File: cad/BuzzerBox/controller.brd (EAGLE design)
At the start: 100 x 100 mm, 132 parts, among them J2 RASPBERRYPI-40-PIN-GPIO_PTH_N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, Q1 BSS138, Q2 BSS138, Q3 BSS138, T1 BC849, T10 BC849, T2 BC849, T3 BC849, T4 BC849, T5 BC849, T6 BC849, T7 BC849, T8 BC849, T9 BC849, U1 ATMEGA328P-AU, Y1 16MHz

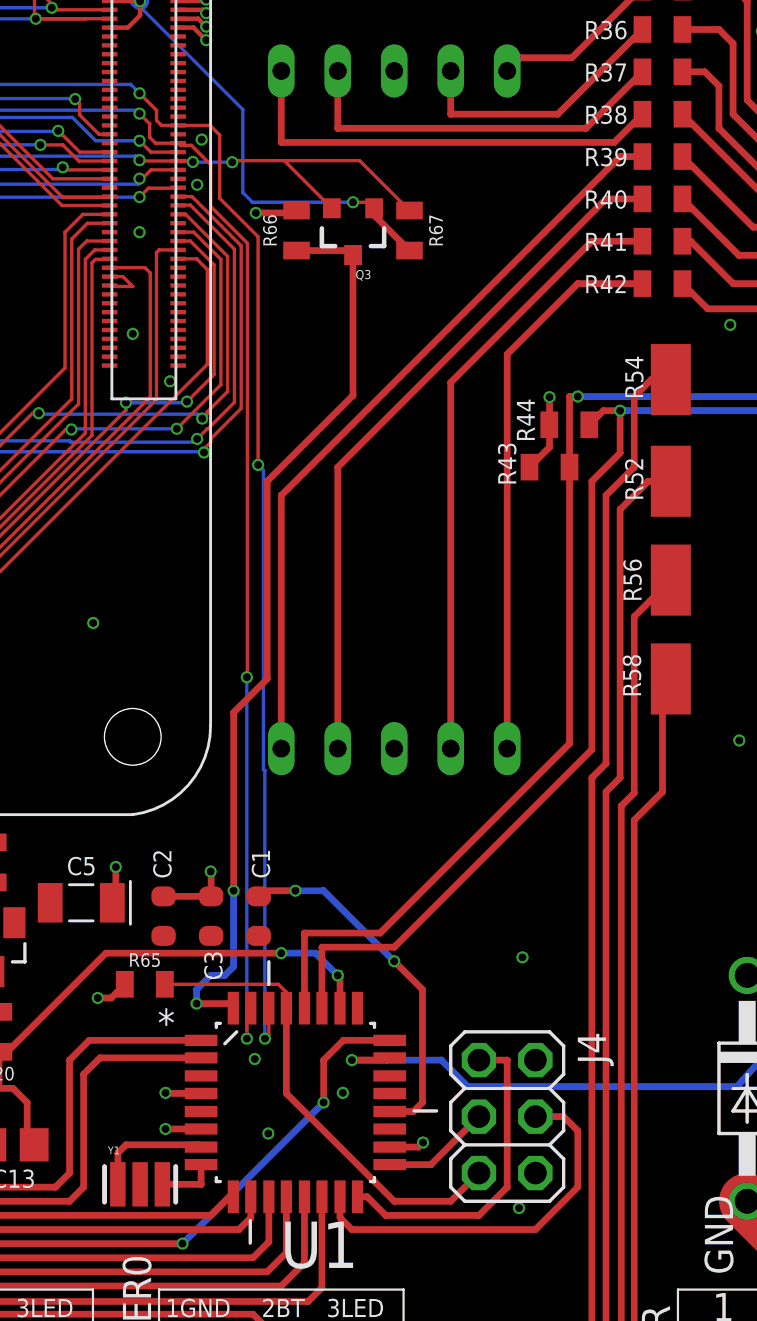
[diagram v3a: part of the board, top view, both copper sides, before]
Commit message: Add level shifter for TX/RX
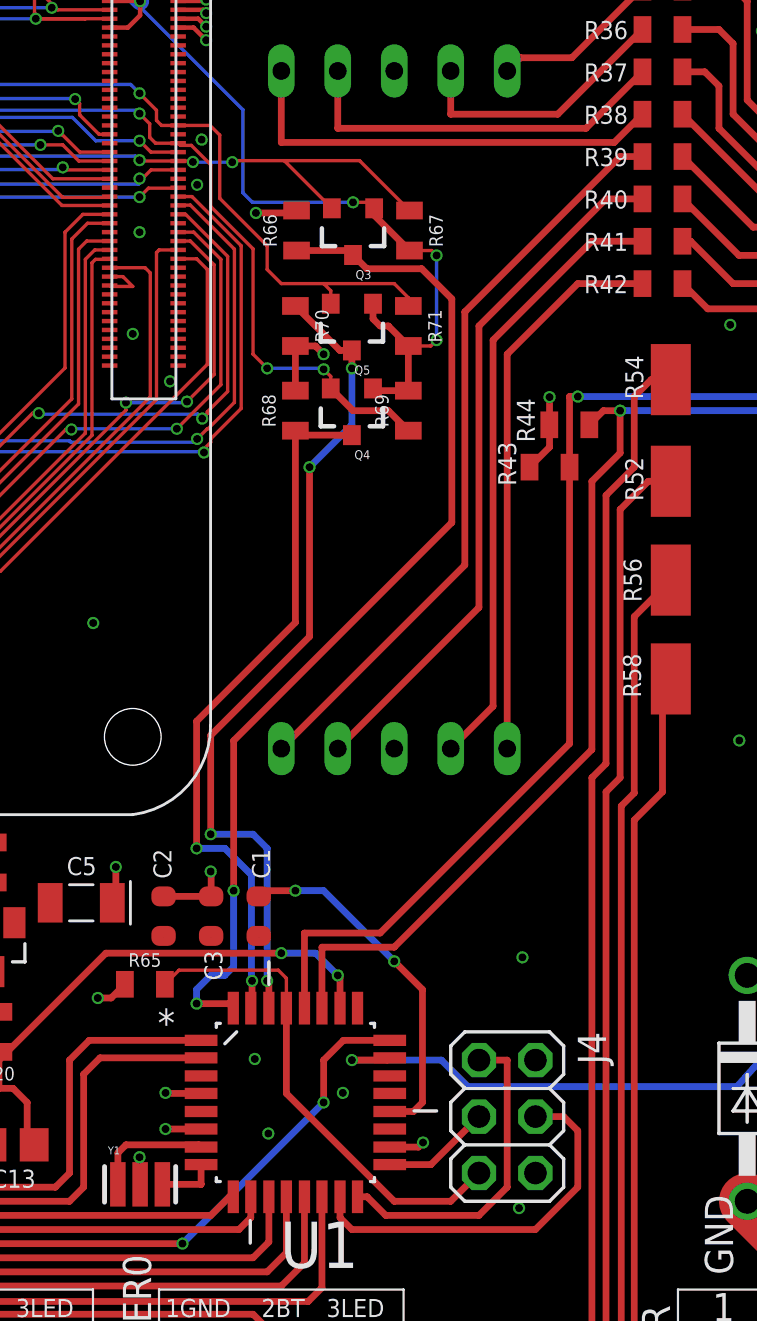
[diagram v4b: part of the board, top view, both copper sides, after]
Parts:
- added Q4, Q5: BSS138, SparkFun:SOT23-3
- added R68, R69, R70, R71: 10K, SparkFun-Resistors:0805
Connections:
- new net RX: Q5.3, R70.1, U1.30
- new net TX: Q4.3, R68.1, U1.31
- net +3V3: now also Q4.1, Q5.1, R69.2, R71.2
- net +5V: now also R68.2, R70.2
- net RXD: now also J2.10, Q4.2, R69.1, RPI-CM4.51; no longer J2.8, RPI-CM4.55, U1.30
- net TXD: now also J2.8, Q5.2, R71.1, RPI-CM4.55; no longer J2.10, RPI-CM4.51, U1.31
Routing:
- net RX: track 0.00 -> 37.8 mm, vias 0 -> 4
- net TX: track 0.00 -> 32.2 mm, vias 0 -> 2
- net RXD: track 95.2 -> 69.5 mm
- net TXD: track 92.9 -> 67.4 mm, vias 3 -> 1
- net +3V3: track 165.0 -> 177.9 mm, vias 5 -> 7
- net D2: track 41.3 -> 46.4 mm
- net +5V: track 101.0 -> 104.5 mm, vias 46 -> 47
- net GND: track 9.94 -> 11.2 mm, vias 46 -> 47
- net RESET: track 21.4 -> 22.3 mm

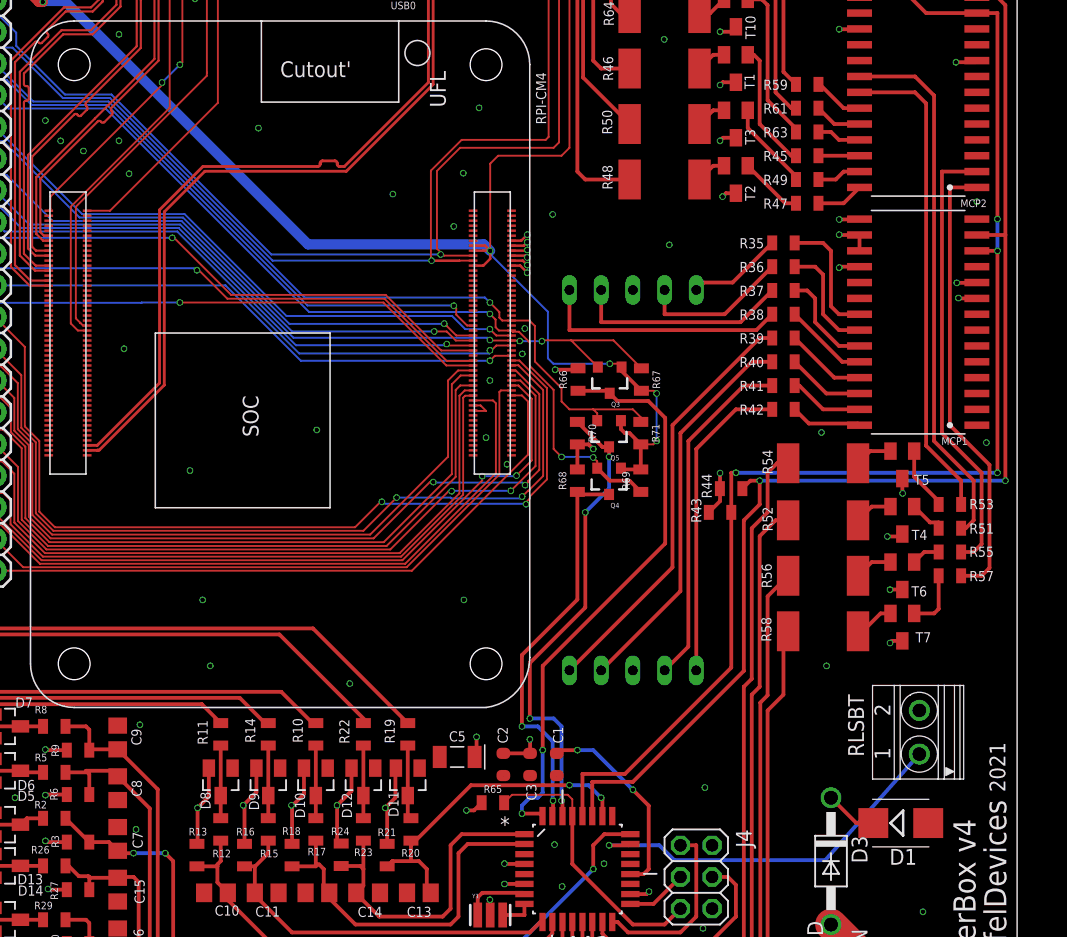
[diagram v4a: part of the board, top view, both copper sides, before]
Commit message: Add input stage for Release button
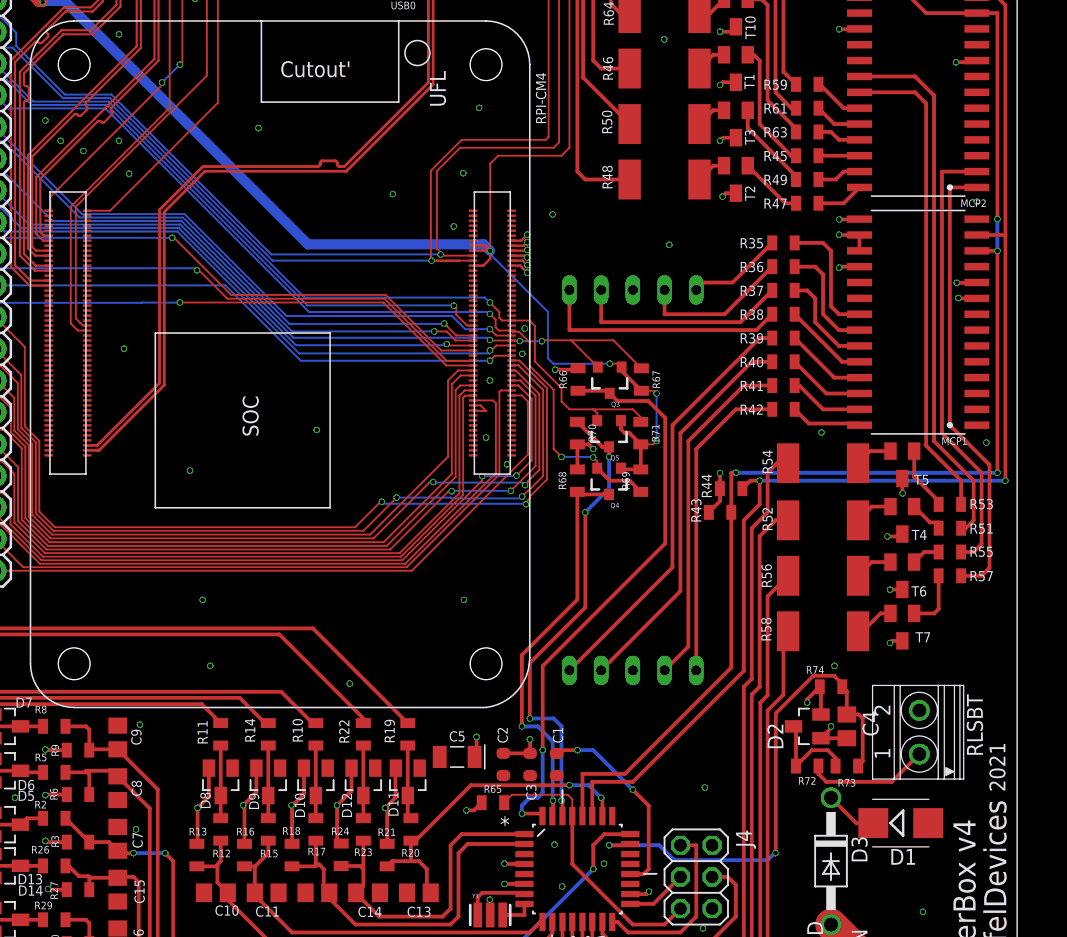
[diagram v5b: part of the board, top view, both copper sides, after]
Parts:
- added C4: 100nF, rcl:C0805
- added D2: HSMS-2852, avago:SOT23
- added R72: 10, SparkFun-Resistors:0805
- added R73: 1k, SparkFun-Resistors:0805
- added R74: 100k, SparkFun-Resistors:0805
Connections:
- new net N$41: D2.3, R72.2, R73.1
- new net RLSBT: R72.1, RLSBT.1
- net +5V: now also D2.2, R74.2
- net A0: now also C4.1, R73.2, R74.1; no longer RLSBT.1
- net GND: now also C4.2, D2.1
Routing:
- net A0: track 30.9 -> 41.8 mm, vias 1 -> 2
- net RLSBT: track 0.00 -> 9.90 mm
- net N$41: track 0.00 -> 7.86 mm
- net +5V: track 104.5 -> 108.4 mm, vias 47 -> 48
- net GND: track 11.2 -> 14.5 mm, vias 47 -> 48
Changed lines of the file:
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@@
 <attribute name="MF" value="" x="92.069" y="30.645" size="1.778" layer="27" rot="R90" display="off"/>
 <attribute name="MPN" value="" x="92.069" y="30.645" size="1.778" layer="27" rot="R90" display="off"/>
-<attribute name="NAME" x="86.46" y="33.6765" size="1.27" layer="25" rot="R270"/>
+<attribute name="NAME" x="95.985" y="33.6765" size="1.27" layer="25" rot="R270"/>
 <attribute name="OC_FARNELL" value="unknown" x="92.069" y="30.645" size="1.778" layer="27" rot="R90" display="off"/>
 <attribute name="OC_NEWARK" value="unknown" x="92.069" y="30.645" size="1.778" layer="27" rot="R90" display="off"/>
@@
 <attribute name="PROD_ID" value=" " x="74.295" y="57.785" size="1.778" layer="27" rot="R270" display="off"/>
 <attribute name="VALUE" x="68.961" y="54.61" size="0.6096" layer="27" font="vector" ratio="20" rot="R270" align="top-center"/>
+</element>
+<element name="D2" library="avago" library_urn="urn:adsk.eagle:library:107" package="SOT23" package3d_urn="urn:adsk.eagle:package:4488/1" value="HSMS-2852" x="83.185" y="31.115" smashed="yes" rot="R90">
+<attribute name="NAME" x="81.28" y="29.21" size="1.27" layer="25" rot="R90"/>
+<attribute name="VALUE" x="86.36" y="29.21" size="1.27" layer="27" rot="R90"/>
+</element>
+<element name="R72" library="SparkFun-Resistors" library_urn="urn:adsk.eagle:library:532" package="0805" package3d_urn="urn:adsk.eagle:package:39651/1" value="10" x="83.185" y="27.94" smashed="yes" rot="R180">
+<attribute name="NAME" x="83.185" y="27.051" size="0.6096" layer="25" font="vector" ratio="20" rot="R180" align="bottom-center"/>
+<attribute name="PROD_ID" value=" " x="90.17" y="27.94" size="1.778" layer="27" rot="R180" display="off"/>
+<attribute name="VALUE" x="83.185" y="28.829" size="0.6096" layer="27" font="vector" ratio="20" rot="R180" align="top-center"/>
+</element>
+<element name="R73" library="SparkFun-Resistors" library_urn="urn:adsk.eagle:library:532" package="0805" package3d_urn="urn:adsk.eagle:package:39651/1" value="1k" x="86.36" y="27.94" smashed="yes">
+<attribute name="NAME" x="86.36" y="26.289" size="0.6096" layer="25" font="vector" ratio="20" align="bottom-center"/>
+<attribute name="PROD_ID" value=" " x="86.36" y="30.48" size="1.778" layer="27" display="off"/>
+<attribute name="VALUE" x="86.36" y="27.051" size="0.6096" layer="27" font="vector" ratio="20" align="top-center"/>
+</element>
+<element name="R74" library="SparkFun-Resistors" library_urn="urn:adsk.eagle:library:532" package="0805" package3d_urn="urn:adsk.eagle:package:39651/1" value="100k" x="85.09" y="34.29" smashed="yes" rot="R180">
+<attribute name="NAME" x="83.82" y="35.941" size="0.6096" layer="25" font="vector" ratio="20" rot="R180" align="bottom-center"/>
+<attribute name="PROD_ID" value=" " x="88.265" y="35.56" size="1.778" layer="27" rot="R180" display="off"/>
+<attribute name="VALUE" x="85.09" y="35.179" size="0.6096" layer="27" font="vector" ratio="20" rot="R180" align="top-center"/>
+</element>
+<element name="C4" library="rcl" library_urn="urn:adsk.eagle:library:334" package="C0805" package3d_urn="urn:adsk.eagle:package:23617/2" value="100nF" x="86.36" y="31.115" smashed="yes" rot="R270">
+<attribute name="NAME" x="87.63" y="32.385" size="1.27" layer="25" rot="R270"/>
+<attribute name="POPULARITY" value="88" x="74.93" y="31.115" size="1.778" layer="27" rot="R270" display="off"/>
+<attribute name="SPICEPREFIX" value="C" x="74.93" y="31.115" size="1.778" layer="27" rot="R270" display="off"/>
+<attribute name="VALUE" x="83.82" y="32.385" size="1.27" layer="27" rot="R270"/>
 </element>
 </elements>
@@
 <via x="15.24" y="17.4752" extent="1-16" drill="0.35"/>
 <via x="84.328" y="54.6608" extent="1-16" drill="0.35"/>
-<via x="84.7344" y="35.9664" extent="1-16" drill="0.35"/>
+<via x="85.3694" y="35.9664" extent="1-16" drill="0.35"/>
 <via x="49.9872" y="73.7616" extent="1-16" drill="0.35"/>
 <via x="56.896" y="80.6704" extent="1-16" drill="0.35"/>
@@
 <wire x1="57.7596" y1="17.2212" x2="57.7596" y2="16.0274" width="0.3048" layer="1"/>
 <via x="57.7596" y="17.2212" extent="1-16" drill="0.35"/>
+<contactref element="D2" pad="1"/>
+<contactref element="C4" pad="2"/>
+<wire x1="84.285" y1="30.165" x2="86.36" y2="30.165" width="0.3048" layer="1"/>
+<wire x1="84.285" y1="30.165" x2="85.09" y2="30.97" width="0.3048" layer="1"/>
+<wire x1="85.09" y1="30.97" x2="85.09" y2="31.115" width="0.3048" layer="1"/>
+<via x="85.09" y="31.115" extent="1-16" drill="0.35"/>
 </signal>
 <signal name="D10">
@@
 <wire x1="65.67" y1="53.71" x2="66.04" y2="53.34" width="0.3048" layer="1"/>
 <via x="66.04" y="53.34" extent="1-16" drill="0.35"/>
+<contactref element="D2" pad="2"/>
+<contactref element="R74" pad="2"/>
+<wire x1="84.285" y1="32.065" x2="84.285" y2="34.195" width="0.3048" layer="1"/>
+<wire x1="84.285" y1="34.195" x2="84.19" y2="34.29" width="0.3048" layer="1"/>
+<wire x1="84.19" y1="34.29" x2="83.185" y2="33.285" width="0.3048" layer="1"/>
+<wire x1="83.185" y1="33.285" x2="83.185" y2="33.02" width="0.3048" layer="1"/>
+<via x="83.185" y="33.02" extent="1-16" drill="0.35"/>
 </signal>
 <signal name="N$45">
@@
 </signal>
 <signal name="A0">
-<contactref element="RLSBT" pad="1"/>
 <contactref element="U1" pad="23"/>
 <wire x1="69.0118" y1="21.6916" x2="68.9102" y2="21.59" width="0.3048" layer="1"/>
@@
 <wire x1="67.31" y1="21.59" x2="71.33670625" y2="21.59" width="0.3048" layer="16"/>
 <wire x1="71.33670625" y1="21.59" x2="72.53050625" y2="20.3962" width="0.3048" layer="16"/>
-<wire x1="72.53050625" y1="20.3962" x2="84.630496875" y2="20.3962" width="0.3048" layer="16"/>
-<wire x1="84.630496875" y1="20.3962" x2="92.169" y2="28.895" width="0.3048" layer="16"/>
+<wire x1="72.53050625" y1="20.3962" x2="80.01" y2="20.3962" width="0.3048" layer="16"/>
+<contactref element="R74" pad="1"/>
+<contactref element="R73" pad="2"/>
+<contactref element="C4" pad="1"/>
+<wire x1="85.99" y1="34.29" x2="86.36" y2="33.92" width="0.3048" layer="1"/>
+<wire x1="86.36" y1="33.92" x2="86.36" y2="32.065" width="0.3048" layer="1"/>
+<wire x1="85.34051875" y1="35.1688875" x2="83.67448125" y2="35.1688875" width="0.3048" layer="1"/>
+<wire x1="85.99" y1="34.29" x2="85.99" y2="34.51940625" width="0.3048" layer="1"/>
+<wire x1="85.99" y1="34.51940625" x2="85.34051875" y2="35.1688875" width="0.3048" layer="1"/>
+<wire x1="83.67448125" y1="35.1688875" x2="80.66989375" y2="32.1643" width="0.3048" layer="1"/>
+<via x="80.645" y="20.955" extent="1-16" drill="0.35"/>
+<wire x1="80.645" y1="20.955" x2="80.5688" y2="20.955" width="0.3048" layer="16"/>
+<wire x1="80.5688" y1="20.955" x2="80.01" y2="20.3962" width="0.3048" layer="16"/>
+<wire x1="80.66989375" y1="32.1643" x2="80.66989375" y2="20.97989375" width="0.3048" layer="1"/>
+<wire x1="80.645" y1="20.955" x2="80.66989375" y2="20.97989375" width="0.3048" layer="1"/>
+<wire x1="86.36" y1="32.065" x2="87.315" y2="32.065" width="0.3048" layer="1"/>
+<wire x1="87.315" y1="32.065" x2="87.63" y2="31.75" width="0.3048" layer="1"/>
+<wire x1="87.63" y1="31.75" x2="87.63" y2="28.31" width="0.3048" layer="1"/>
+<wire x1="87.63" y1="28.31" x2="87.26" y2="27.94" width="0.3048" layer="1"/>
 </signal>
 <signal name="N$1">
@@
 <wire x1="35.0856" y1="83.493984375" x2="35.0856" y2="90.8682" width="0.1524" layer="1"/>
 <wire x1="35.0856" y1="83.493984375" x2="35.077125" y2="83.235525" width="0.1524" layer="1"/>
-<wire x1="24.5872" y1="72.7456" x2="35.077125" y2="83.235525" width="0.1524" layer="1"/>
+<wire x1="35.077125" y1="83.235525" x2="24.5872" y2="72.7456" width="0.1524" layer="1"/>
 </signal>
 <signal name="GP4">
@@
 <wire x1="66.77" y1="53.51" x2="64.77" y2="55.51" width="0.3048" layer="1"/>
 </signal>
+<signal name="N$41">
+<contactref element="R73" pad="1"/>
+<contactref element="D2" pad="3"/>
+<contactref element="R72" pad="2"/>
+<wire x1="82.285" y1="27.94" x2="82.285" y2="30.915" width="0.3048" layer="1"/>
+<wire x1="82.285" y1="30.915" x2="82.085" y2="31.115" width="0.3048" layer="1"/>
+<wire x1="85.46" y1="27.94" x2="85.46" y2="28.575" width="0.3048" layer="1"/>
+<wire x1="85.46" y1="28.575" x2="84.825" y2="29.21" width="0.3048" layer="1"/>
+<wire x1="83.555" y1="29.21" x2="82.285" y2="27.94" width="0.3048" layer="1"/>
+<wire x1="84.825" y1="29.21" x2="83.555" y2="29.21" width="0.3048" layer="1"/>
+</signal>
+<signal name="RLSBT">
+<contactref element="RLSBT" pad="1"/>
+<contactref element="R72" pad="1"/>
+<wire x1="84.72" y1="26.67" x2="84.085" y2="27.305" width="0.3048" layer="1"/>
+<wire x1="84.085" y1="27.94" x2="84.085" y2="27.305" width="0.3048" layer="1"/>
+<wire x1="89.944" y1="26.67" x2="92.169" y2="28.895" width="0.3048" layer="1"/>
+<wire x1="84.72" y1="26.67" x2="89.944" y2="26.67" width="0.3048" layer="1"/>
+</signal>
 </signals>
